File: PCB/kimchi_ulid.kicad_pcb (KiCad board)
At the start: 4 copper layers, 65 x 45.4 mm, 31 parts, among them J1 DF40HC(3.5)-60DS, J2 DF40HC(3.5)-60DS, J4 54-00177, J5 RCJ-2123, J6 RCJ-2123, U1 24C32, U2 SN74LV1T34DBVRG4, U3 SGTL5000XNLA3, X1 ASFL1-12.288MHZ-EC-T

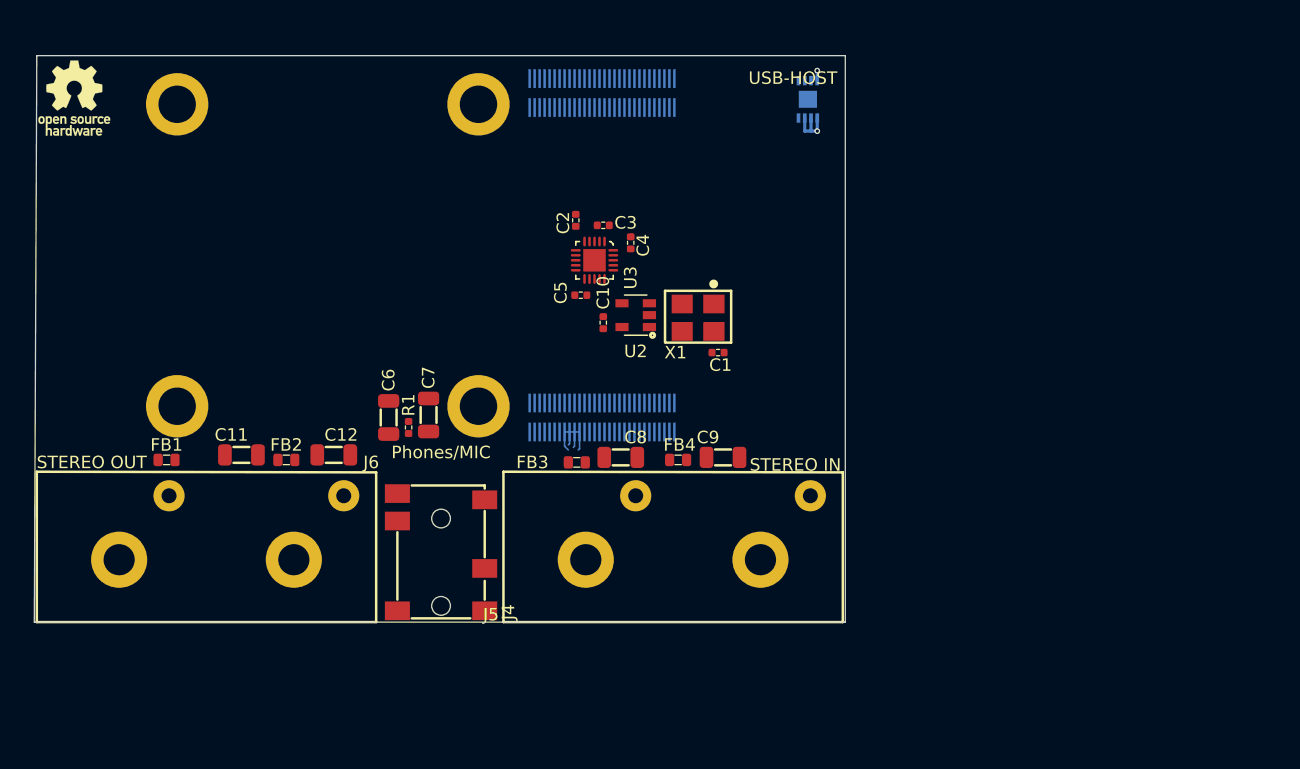
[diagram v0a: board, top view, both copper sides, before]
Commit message: redesigned circuit around WM8750 codec, added needed components to library
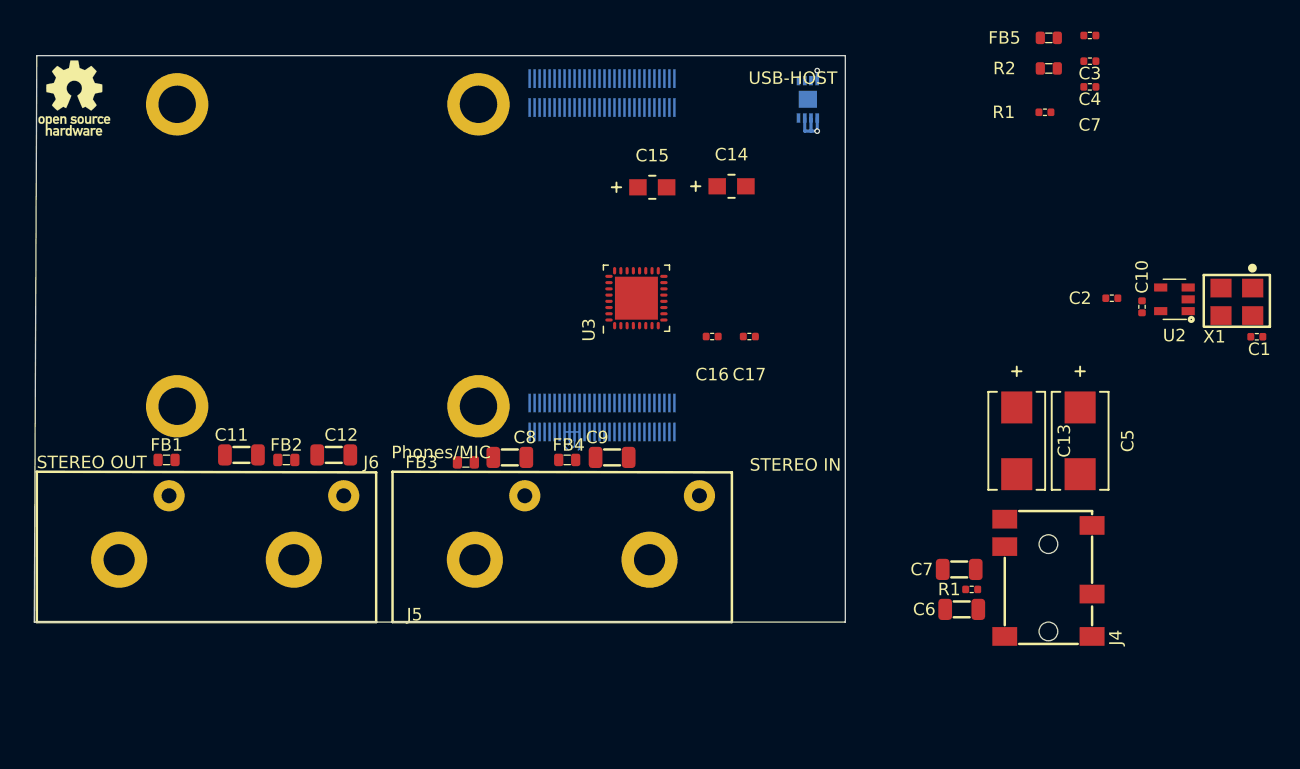
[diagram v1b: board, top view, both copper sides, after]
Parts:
- added C13: T491D227M010AT, kimchi_ulid:T491D227M010AT, F.Cu at (185.7, 101.9)
- added C14: T494A106M006AT, kimchi_ulid:T494A106M006AT, F.Cu at (162.9, 81.5)
- added C15: T494A106M006AT, kimchi_ulid:T494A106M006AT, F.Cu at (156.5, 81.5)
- added C16: C0402C104K9PACTU, kimchi_ulid:C0402, F.Cu at (161.3, 93.5)
- added C17: C0402C104K9PACTU, kimchi_ulid:C0402, F.Cu at (164.3, 93.5)
- added C7: C0402C104K9PACTU, kimchi_ulid:C0402, F.Cu at (191.6, 73.5)
- added FB5: FBMJ1608HM180NTR, kimchi_ulid:R0603, F.Cu at (188.3, 69.6)
- added R1: RC0402JR-072K2L, AVR-KiCAD-Lib-Resistors:R0402, F.Cu at (188.0, 75.5)
- added R2: RC0603FR-0747KL, AVR-KiCAD-Lib-Resistors:R0603, F.Cu at (188.3, 72.0)
- C5: value C0402C104K9PACTU -> T491D227M010AT; footprint kimchi_ulid:C0402 -> kimchi_ulid:T491D227M010AT
- U3: value SGTL5000XNLA3 -> WM8750CJLGEFL; footprint kimchi_ulid:QFN40P300X300X60-21N -> kimchi_ulid:QFN-32_EP_5x5_Pitch0.5mm
- moved J4 48.7 mm to (188.3, 119.7)
- moved C6 48.4 mm to (181.3, 115.4), turned to 0 degrees
- moved R1 47.0 mm to (182.1, 113.8), turned to 0 degrees
- moved C7 44.3 mm to (181.1, 112.2), turned to 180 degrees
- moved C2 43.4 mm to (193.4, 90.4), turned to 0 degrees
- moved C10 43.2 mm to (195.8, 91.1)
- moved U2 43.2 mm to (198.4, 90.5)
- moved X1 43.2 mm to (203.4, 90.7)
- moved C1 43.2 mm to (205.0, 93.5)
- moved C3 41.9 mm to (191.6, 69.4)
- moved C5 41.7 mm to (190.8, 101.9), turned to 270 degrees
- moved C4 39.6 mm to (191.6, 71.4), turned to 0 degrees
- moved C8 8.89 mm to (145.1, 103.2)
- moved C9 8.89 mm to (153.3, 103.2)
- moved FB3 8.89 mm to (141.6, 103.6)
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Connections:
- C2 pad 1: Net-(C2-Pad1) -> VDD_3V3
- C5 pad 1: VDD_3V3 -> Net-(C5-Pad1)
- C5 pad 2: GND -> Net-(C5-Pad2)
- J4 pad 1: GND -> Net-(FB5-Pad2)
- J4 pad 3: HPOUT_R -> Net-(C13-Pad2)
- J4 pad 4: HPOUT_L -> Net-(C5-Pad2)
- U2 pad 4: Net-(U2-Pad4) -> MCLK
- U3 pad 1: HPOUT_L -> MCLK
- U3 pad 10: MIC_IN -> Net-(U3-Pad10)
- U3 pad 11: MIC_BIAS -> Net-(U3-Pad11)
- U3 pad 12: VDD_3V3 -> Net-(C13-Pad1)
- U3 pad 13: Net-(U2-Pad4) -> Net-(C5-Pad1)
- U3 pad 14: Net-(U3-Pad14) -> GND
- U3 pad 15: Net-(U3-Pad15) -> Net-(C12-Pad1)
- U3 pad 16: Net-(U3-Pad16) -> Net-(C11-Pad1)
- U3 pad 17: Net-(U3-Pad17) -> VDD_3V3
- U3 pad 18: Net-(U3-Pad18) -> VDD_3V3
- U3 pad 19: Net-(U3-Pad19) -> GND
- U3 pad 2: GND -> VDD_3V3
- U3 pad 21: GND -> VDD_3V3
- U3 pad 4: HPOUT_R -> GND
- U3 pad 5: Net-(C2-Pad1) -> Net-(U3-Pad5)
- U3 pad 6: Net-(C9-Pad1) -> Net-(U3-Pad6)
- U3 pad 7: Net-(C8-Pad1) -> Net-(U3-Pad7)
- U3 pad 8: Net-(C12-Pad1) -> Net-(U3-Pad8)
- U3 pad 9: Net-(C11-Pad1) -> Net-(U3-Pad9)

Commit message: Route In Progress
Now doing the intial route of the board, still very much a work in progress, have the pwoer planes figured out and general component placenment. All components now have 3D models.
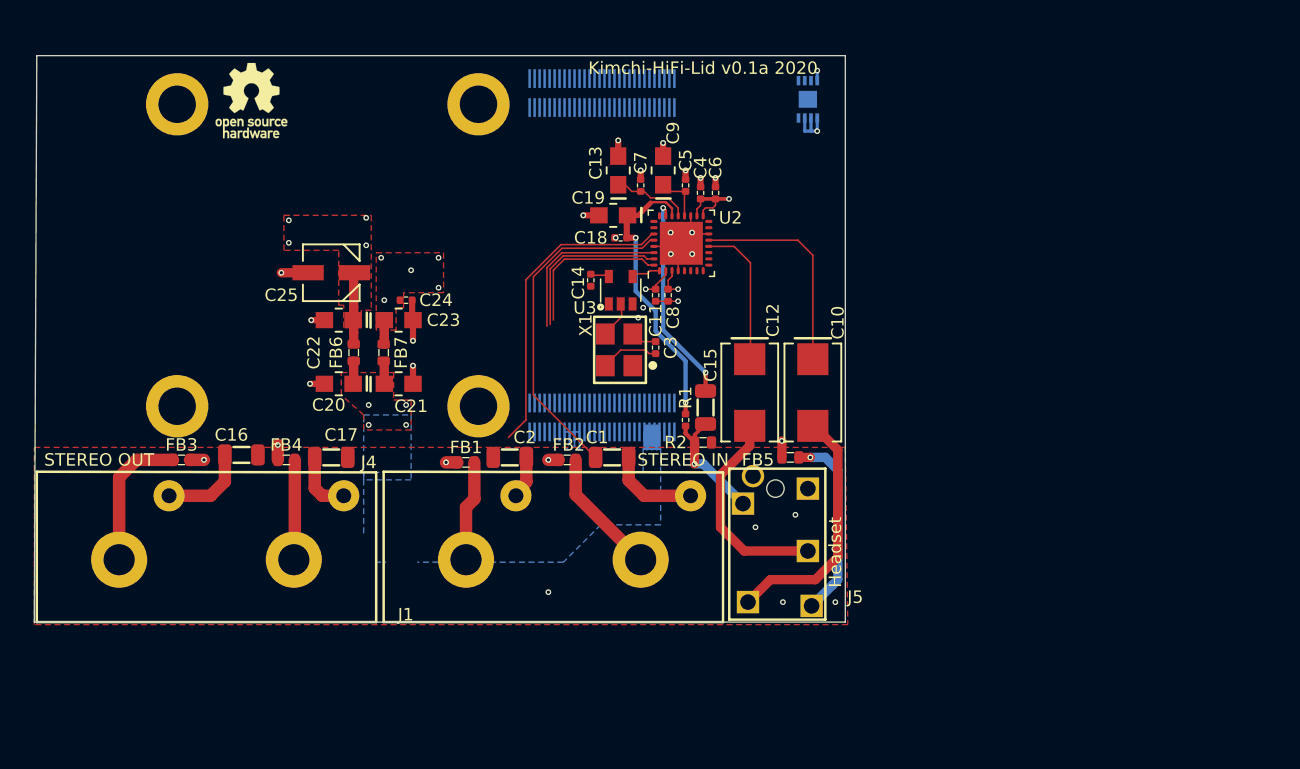
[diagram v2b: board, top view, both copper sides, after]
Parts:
- removed the C7 at (181.1, 112.2)
- removed the J4 at (188.3, 119.7)
- removed the R1 at (182.1, 113.8)
- added C18: C0402C104K9PACTU, kimchi_ulid:C0402, F.Cu at (154.0, 85.6)
- added C19: T494A106M006AT, kimchi_ulid:T494A106M006AT, F.Cu at (153.4, 83.8)
- added C20: T494A106M006AT, kimchi_ulid:T494A106M006AT, F.Cu at (131.4, 97.3)
- added C21: T494A106M006AT, kimchi_ulid:T494A106M006AT, F.Cu at (136.2, 97.3)
- added C22: T494A106M006AT, kimchi_ulid:T494A106M006AT, F.Cu at (131.4, 92.2)
- added C23: T494A106M006AT, kimchi_ulid:T494A106M006AT, F.Cu at (136.2, 92.2)
- added C24: C0402C104K9PACTU, kimchi_ulid:C0402, F.Cu at (136.8, 90.6)
- added C25: UZP1H0R1MCL1GB, kimchi_ulid:UZP1H0R1MCL1GB, F.Cu at (130.8, 88.4)
- added FB6: FBMJ1608HM180NTR, kimchi_ulid:R0603, F.Cu at (132.6, 94.8)
- added FB7: FBMJ1608HM180NTR, kimchi_ulid:R0603, F.Cu at (135.0, 94.8)
- added J5: 54-00176, kimchi_ulid:54-00176, F.Cu at (166.4, 116.2)
- moved X1 49.7 mm to (153.9, 94.6), turned to 90 degrees
- moved C3 48.2 mm to (156.8, 94.4), turned to 90 degrees
- moved U3 44.4 mm to (154.0, 89.8), turned to 90 degrees
- moved C14 44.2 mm to (151.6, 89.0), turned to 270 degrees
- moved R2 40.8 mm to (160.6, 102.0), turned to 180 degrees
- moved FB5 39.5 mm to (167.6, 103.2)
- moved C8 38.7 mm to (157.8, 90.2), turned to 270 degrees
- moved C11 38.6 mm to (156.8, 90.2), turned to 270 degrees
- moved R1 37.9 mm to (159.2, 100.2), turned to 90 degrees
- moved C4 34.0 mm to (160.4, 82.0), turned to 90 degrees
- moved C6 32.5 mm to (161.6, 82.0), turned to 90 degrees
- moved C15 26.1 mm to (160.8, 99.2), turned to 270 degrees
- moved C10 21.8 mm to (169.4, 98.0)
- moved C12 21.7 mm to (164.3, 98.0)
- moved C7 14.9 mm to (155.6, 81.4), turned to 90 degrees
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- renumbered C9 to C1, C5 to C10, C7 to C11, C13 to C12, C15 to C13, C10 to C14, C6 to C15, C11 to C16, C12 to C17, C8 to C2, C1 to C3, C2 to C4, C16 to C5, C3 to C6, C17 to C7, C4 to C8, C14 to C9, FB3 to FB1, FB4 to FB2, FB1 to FB3, FB2 to FB4, H3 to H2, H2 to H3, J5 to J1, J1 to J2, J2 to J3, J6 to J4, U3 to U2, U2 to U3
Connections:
- C11 pad 1: VDD_3V3 -> VDD
- C13 pad 1: VDD_3V3 -> Net-(C13-Pad1)
- C14 pad 1: VDD_3V3 -> VDD
- C3 pad 1: VDD_3V3 -> VDD
- C4 pad 1: VDD_3V3 -> VDDA
- C5 pad 1: VDD_3V3 -> Net-(C5-Pad1)
- C6 pad 1: VDD_3V3 -> VDDA
- C7 pad 1: VDD_3V3 -> Net-(C13-Pad1)
- C8 pad 1: VDD_3V3 -> VDD
- C9 pad 1: VDD_3V3 -> Net-(C5-Pad1)
- J3 pad 59: PCIE_USB_D_P -> USB2_DP
- J3 pad 60: PCIE_USB_D_N -> USB2_DN
- U2 pad 17: VDD_3V3 -> VDDA
- U2 pad 18: VDD_3V3 -> VDDA
- U2 pad 2: VDD_3V3 -> VDD
- U2 pad 20: VDD_3V3 -> Net-(C5-Pad1)
- U2 pad 21: VDD_3V3 -> Net-(C13-Pad1)
- U2 pad 3: VDD_3V3 -> VDD
- U3 pad 5: VDD_3V3 -> VDD
- X1 pad 4: VDD_3V3 -> VDD
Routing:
- net GND: track 6.61 -> 37.3 mm, vias 0 -> 30
- net Net-(C1-Pad1): track 0.00 -> 27.4 mm
- net Net-(C2-Pad1): track 0.00 -> 25.0 mm
- net MIC_BIAS: track 0.00 -> 23.4 mm, vias 0 -> 2
- net Net-(C10-Pad2): track 0.00 -> 21.8 mm
- net Net-(C10-Pad1): track 0.00 -> 17.2 mm
- net Net-(C12-Pad2): track 0.00 -> 17.0 mm
- net MIC_IN: track 0.00 -> 16.8 mm, vias 0 -> 2
- net VDD_3V3: track 4.95 -> 20.5 mm, vias 2 -> 6
- net Net-(FB5-Pad2): track 0.00 -> 15.3 mm, vias 0 -> 1
- net I2S_CSB: track 0.00 -> 13.8 mm
- net I2S_SDIN: track 0.00 -> 13.3 mm
- net VDD: track 0.00 -> 13.2 mm, vias 0 -> 7
- net I2S_SCLK: track 0.00 -> 12.6 mm
- net Net-(C12-Pad1): track 0.00 -> 11.6 mm
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- added copper zone on F.Cu, net GND
- added copper zone on F.Cu, net VDD
- added copper zone on In2.Cu, net VDD
- added copper zone on F.Cu, net VDDA
- added copper zone on In2.Cu, net VDDA
- added copper zone on B.Cu, net VDD_3V3
- added copper zone on F.Cu, net VDD_3V3
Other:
- board text added: "Headset"
- board text added: "Kimchi-HiFi-Lid v0.1a 2020"
- board text removed: "Phones/MIC"
- board text removed: "USB-HOST"

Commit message: First Route Pass Completed
Completed first pass of routting the board. Need to adjust trace width for analog front ends for audio in and out.
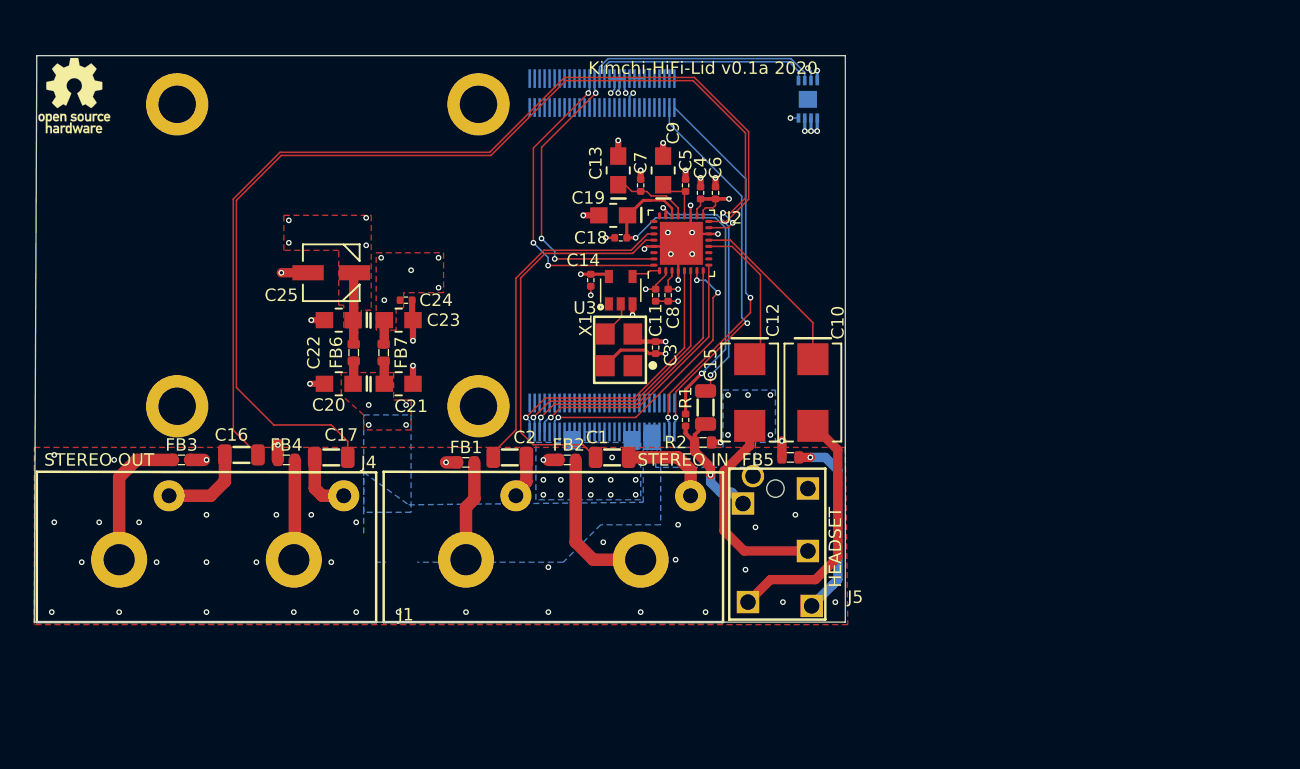
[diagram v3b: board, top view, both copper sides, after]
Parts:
- moved LOGO1 14.2 mm to (110.2, 74.2)
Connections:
- net I2S_CSB renamed Net-(U2-Pad30)
- U2 pad 31: I2S_SDIN -> I2C3_SDA
- U2 pad 32: I2S_SCLK -> I2C3_SCL
- U2 pad 5: Net-(U2-Pad5) -> SAI3_TXC
- U2 pad 6: Net-(U2-Pad6) -> SAI3_TXD
- U2 pad 7: Net-(U2-Pad7) -> SAI3_TXFS
- U2 pad 8: Net-(U2-Pad8) -> SAI3_RXD
- U2 pad 9: Net-(U2-Pad9) -> SAI3_RXFS
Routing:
- net Net-(C17-Pad1): track 0.00 -> 84.2 mm, vias 0 -> 2
- net Net-(C16-Pad1): track 0.00 -> 77.8 mm
- net GND: track 37.3 -> 75.6 mm, vias 30 -> 81
- net USB2_DP: track 0.00 -> 31.3 mm, vias 0 -> 2
- net USB2_DN: track 0.00 -> 31.1 mm, vias 0 -> 2
- net I2C3_SCL: track 0.00 -> 25.8 mm, vias 0 -> 3
- net I2C3_SDA: track 0.00 -> 24.7 mm, vias 0 -> 3
- net SAI3_TXFS: track 0.00 -> 23.1 mm, vias 0 -> 3
- net SAI3_RXFS: track 0.00 -> 22.5 mm, vias 0 -> 1
- net SAI3_TXC: track 0.00 -> 22.5 mm, vias 0 -> 1
- net SAI3_RXD: track 0.00 -> 22.2 mm, vias 0 -> 1
- net SAI3_TXD: track 0.00 -> 22.2 mm, vias 0 -> 1
- net I2C4_SCL: track 0.00 -> 18.8 mm
- net I2C4_SDA: track 0.00 -> 17.7 mm
- net Net-(U2-Pad30): track 13.8 -> 0.00 mm
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- added copper zone on B.Cu, net GND
- added copper zone on In2.Cu, net VDD_3V3
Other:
- board text added: "HEADSET"
- board text removed: "Headset"

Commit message: MCLK Jumper
MCLK jumper added, trace width tweaked and DRC passed.
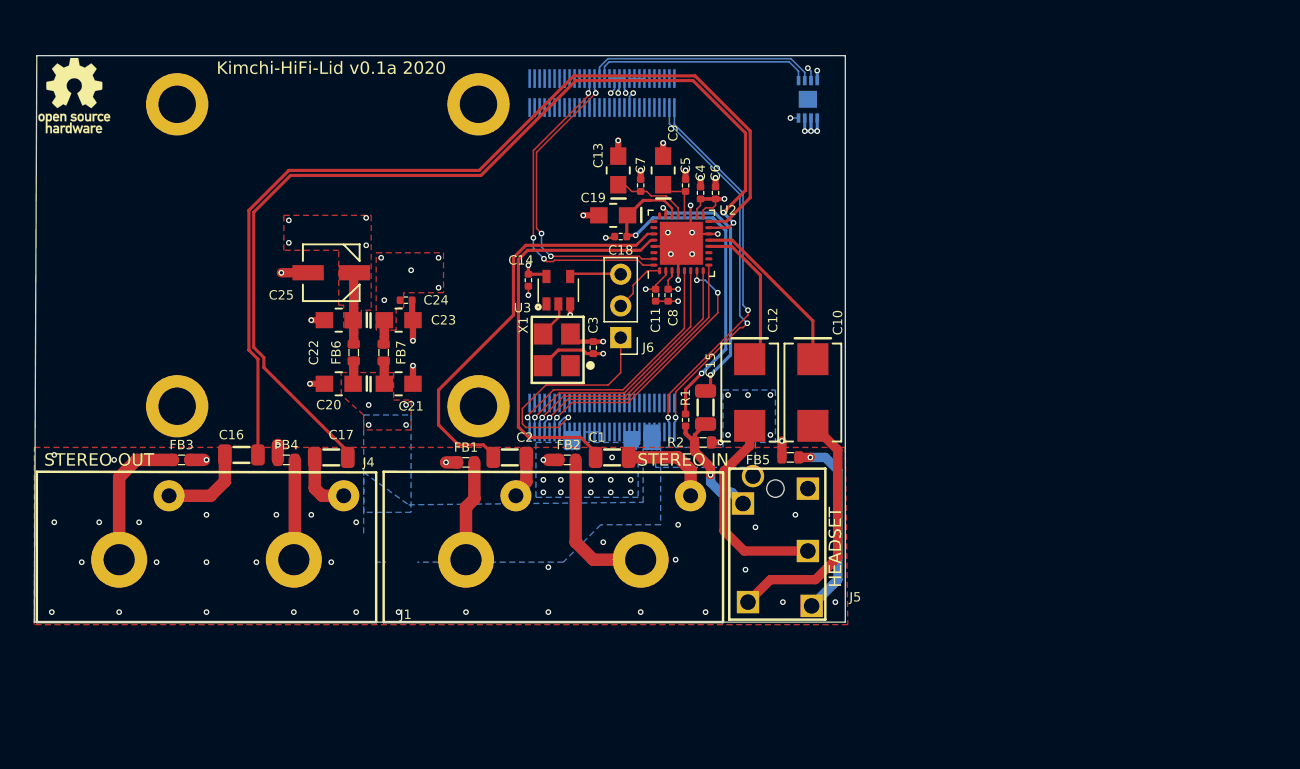
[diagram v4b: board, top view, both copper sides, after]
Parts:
- added J6: Conn_01x03_Male, Pin_Headers:Pin_Header_Straight_1x03_Pitch2.54mm, F.Cu at (154.0, 93.6)
- moved C14 5.00 mm to (146.6, 89.0)
- moved C3 5.00 mm to (151.8, 94.4)
- moved U3 5.00 mm to (149.0, 89.8)
- moved X1 5.00 mm to (148.9, 94.6)
- moved C18 0.10 mm to (154.0, 85.5)
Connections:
- U2 pad 1: MCLK -> Net-(J6-Pad2)
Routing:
- net SAI3_MCLK: track 0.00 -> 18.9 mm, vias 0 -> 1
- net Net-(C2-Pad1): track 27.6 -> 33.5 mm
- net Net-(C17-Pad1): track 84.2 -> 78.7 mm
- net Net-(J6-Pad2): track 0.00 -> 4.66 mm
- net Net-(C16-Pad1): track 77.8 -> 75.8 mm
- net MCLK: track 2.19 -> 4.00 mm
- net Net-(C1-Pad1): track 31.1 -> 32.4 mm
- net GND: track 75.6 -> 74.4 mm, vias 81 -> 80
- net SAI3_TXD: track 22.2 -> 21.2 mm
- net SAI3_TXC: track 22.5 -> 21.5 mm
- net SAI3_TXFS: track 23.1 -> 22.1 mm
- net SAI3_RXD: track 22.2 -> 21.3 mm
- net SAI3_RXFS: track 22.5 -> 21.6 mm

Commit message: MCLK Traces
MCLK trace moved
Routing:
- net SAI3_MCLK: track 18.9 -> 17.1 mm, vias 1 -> 3
- net SAI3_TXFS: track 22.1 -> 22.8 mm
- net SAI3_RXFS: track 21.6 -> 22.2 mm
